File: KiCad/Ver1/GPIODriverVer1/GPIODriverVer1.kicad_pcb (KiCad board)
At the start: 4 copper layers, 176 parts, among them J1 Conn_01x22_Male, J2 GPIODriveOutputs, Q1 DTC143EE, Q10 2N7002, Q11 BSS84, Q12 2N7002, Q13 DTC143EE, Q14 DTC143EE, Q15 DTC143EE, Q16 DTC143EE, Q17 BSS84, Q18 2N7002, Q19 BSS84, Q2 DTC143EE, Q20 2N7002, Q21 BSS84, Q22 2N7002, Q23 BSS84, Q24 2N7002, Q25 2N7002, Q26 2N7002, Q27 2N7002, Q28 2N7002, Q29 2N7002, Q3 DTC143EE, Q30 2N7002, Q31 2N7002, Q32 2N7002, Q4 DTC143EE, Q5 BSS84, Q6 2N7002, Q7 BSS84, Q8 2N7002, Q9 BSS84, U1 74HC244, U2 74HC244, U3 NCV8452, U4 74HC595_Nexperia, U5 74HC595_Nexperia, U6 74HC165

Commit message: Save progress for this week
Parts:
- added REF**: MountingHole_3.2mm_M3_Pad_Via, MountingHole:MountingHole_3.2mm_M3_Pad_Via, F.Cu at (121.2, 125.5)
- added REF**: MountingHole_3.2mm_M3_Pad_Via, MountingHole:MountingHole_3.2mm_M3_Pad_Via, F.Cu at (161.2, 125.5)
- added REF**: MountingHole_3.2mm_M3_Pad_Via, MountingHole:MountingHole_3.2mm_M3_Pad_Via, F.Cu at (121.2, 85.5)
- added REF**: MountingHole_3.2mm_M3_Pad_Via, MountingHole:MountingHole_3.2mm_M3_Pad_Via, F.Cu at (161.2, 85.5)
- Q10, Q12, Q18, Q20, Q22, Q24, Q6, Q8, R29, R30, R31, R32, R34, R36, R38, R40, R53, R54, R55, R56, R58, R60, R62, R64: moved to B.Cu
- moved R64 411.5 mm to (200.8, 167.2), turned to 180 degrees
- moved Q22 408.7 mm to (197.0, 154.8), turned to 180 degrees
- moved Q24 408.4 mm to (196.5, 165.5), turned to 180 degrees
- moved R56 402.5 mm to (201.0, 164.8), turned to 180 degrees
- moved R62 388.5 mm to (201.2, 156.2), turned to 180 degrees
- moved R55 385.2 mm to (201.5, 154.0), turned to 180 degrees
- moved R60 378.7 mm to (201.0, 144.5), turned to 180 degrees
- moved Q20 378.3 mm to (197.0, 143.5), turned to 180 degrees
- moved R58 371.5 mm to (200.0, 129.5), turned to 180 degrees
- moved R53 371.5 mm to (199.8, 126.5), turned to 180 degrees
- moved R54 371.1 mm to (201.5, 141.8), turned to 180 degrees
- moved R45 368.9 mm to (149.2, 120.5), turned to 180 degrees
- moved D23 368.0 mm to (147.0, 119.0)
- moved Q21 367.5 mm to (150.5, 118.5)
- moved Q18 367.1 mm to (196.5, 127.8), turned to 180 degrees
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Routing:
- net VDrive: track 0.00 -> 38.7 mm
- net /DriveSense/D7_In: track 0.00 -> 24.3 mm
- net /DriveSense/D0_In: track 0.00 -> 22.9 mm
- net /DriveSense/D6_In: track 0.00 -> 21.2 mm
- net /DriveSense/D1_In: track 0.00 -> 19.7 mm
- net Net-(D19-Pad2): track 0.00 -> 18.6 mm
- net /DriveSense/D5_In: track 0.00 -> 17.6 mm
- net /DriveSense/D2_In: track 0.00 -> 16.0 mm
- net Net-(D1-Pad2): track 0.00 -> 15.7 mm
- net Net-(D17-Pad2): track 0.00 -> 15.4 mm
- net /DriveSense/D4_In: track 0.00 -> 14.7 mm
- net /DriveSense/D3_In: track 0.00 -> 14.1 mm
- net Net-(D15-Pad2): track 0.00 -> 12.0 mm
- net Net-(D3-Pad2): track 0.00 -> 11.8 mm
- net Net-(D12-Pad2): track 0.00 -> 10.3 mm
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
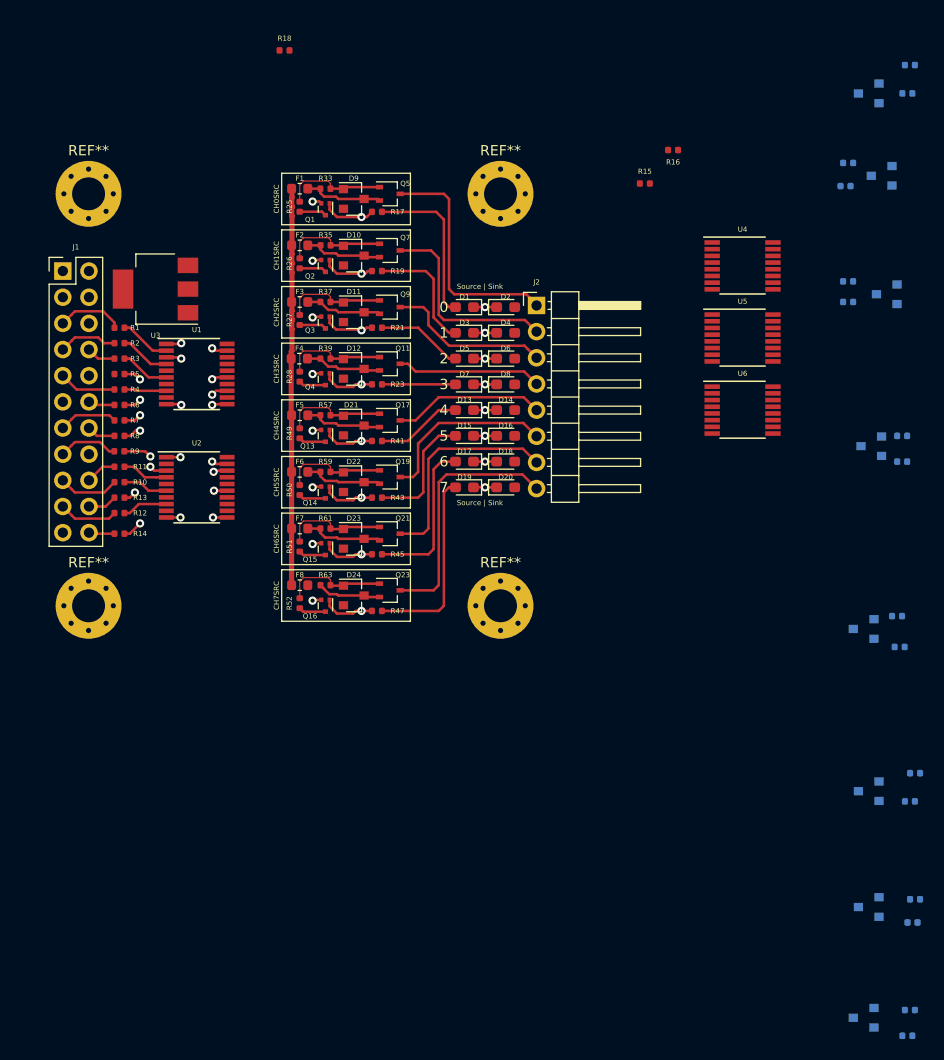
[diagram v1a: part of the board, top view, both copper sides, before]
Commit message: Updated board with possible sink driver layout.
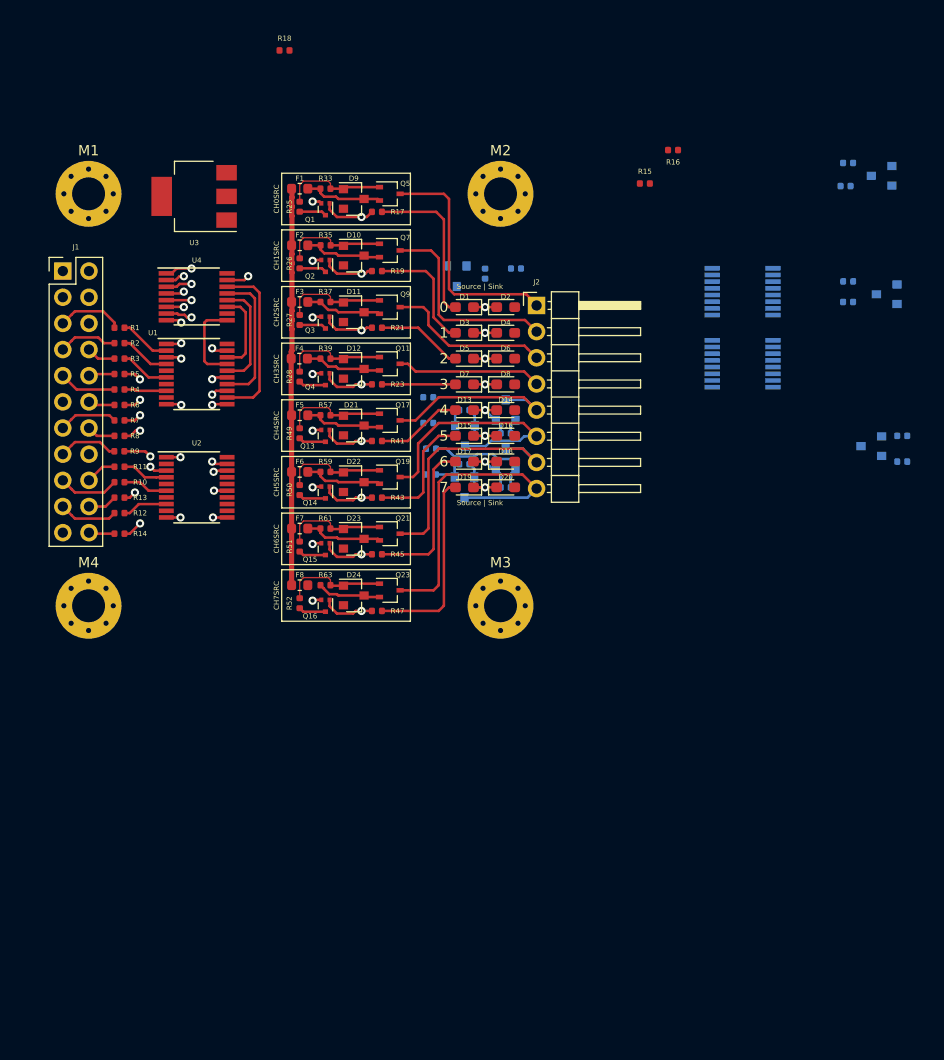
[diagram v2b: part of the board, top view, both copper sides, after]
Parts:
- U5, U6: moved to B.Cu
- moved R64 70.2 mm to (157.7, 111.8)
- moved R56 69.8 mm to (154.5, 112.8)
- moved Q24 64.5 mm to (157.8, 114.0), turned to 270 degrees
- moved R55 64.2 mm to (154.5, 110.2)
- moved R54 58.2 mm to (154.2, 107.8)
- moved R62 57.8 mm to (161.8, 114.0), turned to 0 degrees
- moved R60 57.6 mm to (157.7, 106.5)
- moved Q22 56.0 mm to (161.8, 111.2), turned to 90 degrees
- moved U4 53.1 mm to (131.8, 95.5)
- moved Q20 52.2 mm to (157.8, 109.0), turned to 270 degrees
- moved R53 50.2 mm to (154.2, 105.2)
- moved R34 46.0 mm to (159.8, 93.2), turned to 90 degrees
- moved Q6 43.8 mm to (157.0, 93.5), turned to 270 degrees
- moved R58 43.5 mm to (161.8, 108.8), turned to 0 degrees
- moved R29 41.6 mm to (162.8, 92.8), turned to 0 degrees
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- renumbered REF** to M1, REF** to M2, REF** to M3, REF** to M4
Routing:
- net /OutputDrive/D7_Source: track 5.12 -> 50.7 mm, vias 1 -> 2
- net /OutputDrive/D6_Source: track 5.12 -> 46.3 mm, vias 1 -> 2
- net /OutputDrive/D5_Source: track 5.12 -> 41.5 mm, vias 1 -> 2
- net /OutputDrive/D4_Source: track 5.12 -> 37.0 mm, vias 1 -> 2
- net /OutputDrive/D3_Source: track 5.12 -> 32.5 mm, vias 1 -> 2
- net /OutputDrive/D2_Source: track 5.06 -> 28.2 mm, vias 1 -> 2
- net /OutputDrive/D1_Source: track 5.12 -> 25.5 mm, vias 1 -> 2
- net /OutputDrive/D0_Source: track 5.23 -> 23.3 mm, vias 1 -> 2
- net SrcDriver_DataIn: track 0.00 -> 16.3 mm
- net GND: track 35.3 -> 50.1 mm, vias 23 -> 24
- net SrcDriver_OE: track 0.00 -> 13.6 mm
- net Net-(Q22-Pad1): track 0.00 -> 11.0 mm
- net SrcDriver_LAT: track 0.00 -> 10.6 mm
- net SrcDriver_DataOut: track 0.00 -> 8.36 mm
- net SR_CLK: track 0.00 -> 7.97 mm
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
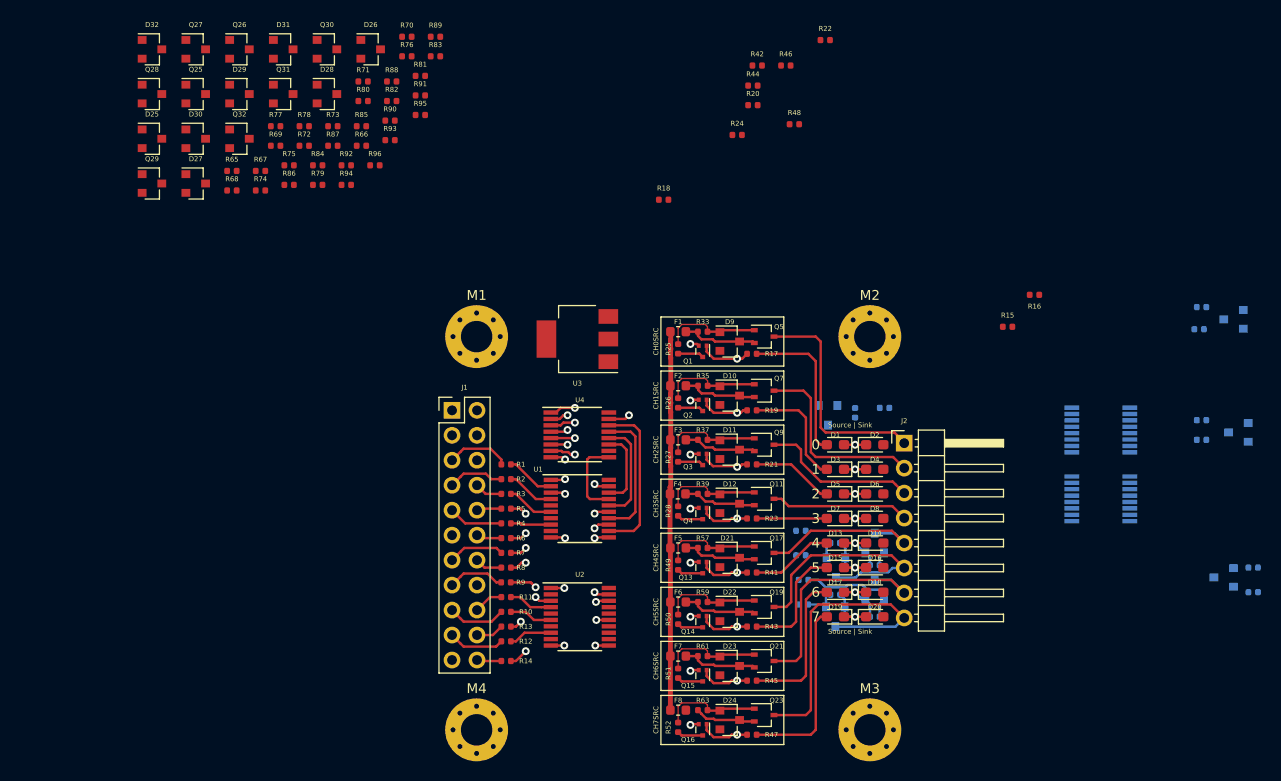
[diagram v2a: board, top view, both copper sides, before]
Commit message: Routed the current sink driver primitives.
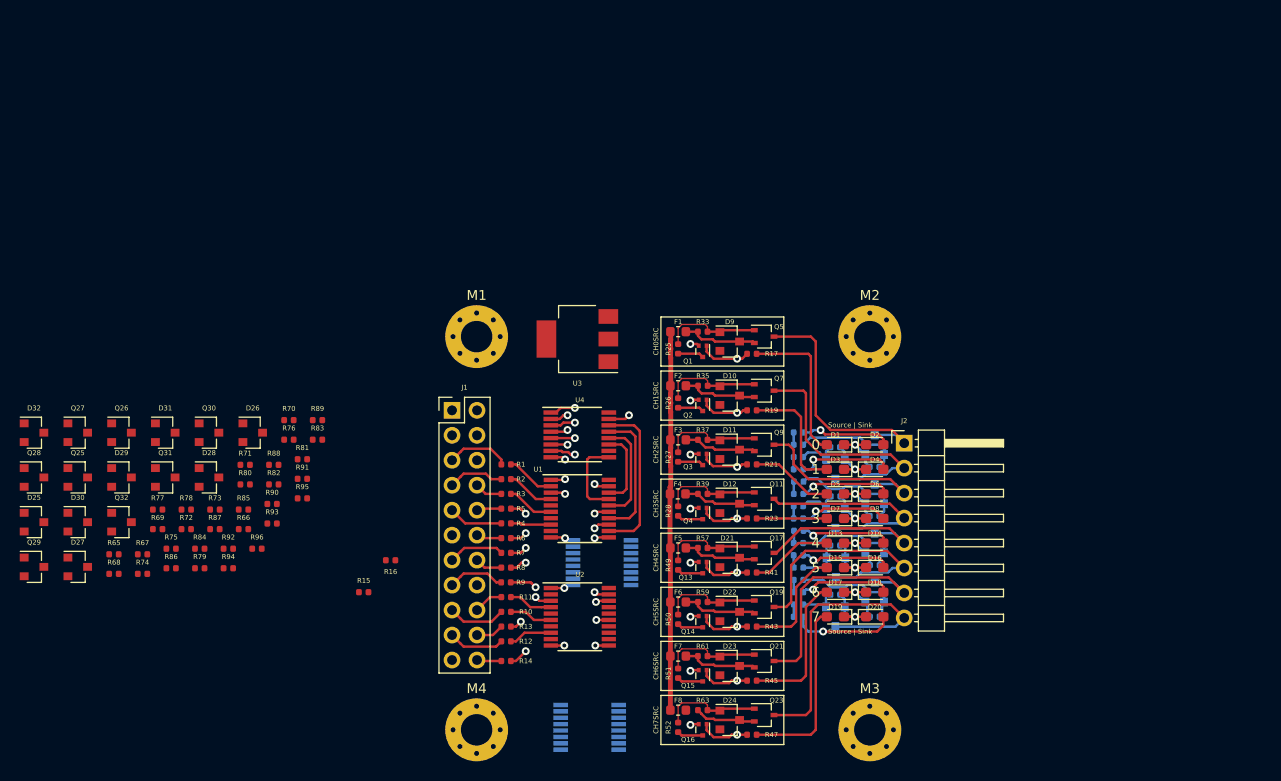
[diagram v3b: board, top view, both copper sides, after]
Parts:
- R18, R20, R22, R24, R42, R44, R46, R48: moved to B.Cu
- moved R16 70.8 mm to (112.5, 108.2)
- moved R15 70.8 mm to (109.8, 111.5)
- moved U5 57.0 mm to (132.8, 125.2)
- moved R46 53.6 mm to (154.0, 111.5), turned to 180 degrees
- moved U6 52.5 mm to (134.0, 108.5)
- moved R48 50.1 mm to (154.0, 114.0), turned to 180 degrees
- moved R44 48.0 mm to (154.0, 107.8), turned to 180 degrees
- moved R42 47.5 mm to (154.0, 105.2), turned to 180 degrees
- moved R32 46.7 mm to (154.0, 102.8)
- moved R22 46.2 mm to (154.0, 101.5), turned to 180 degrees
- moved R30 43.8 mm to (154.0, 97.8)
- moved R40 43.6 mm to (157.8, 101.8)
- moved Q8 43.3 mm to (157.8, 99.0), turned to 270 degrees
- moved R31 41.5 mm to (154.0, 100.2)
- moved R81 40.8 mm to (103.5, 98.0)
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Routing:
- net GND: track 50.1 -> 61.9 mm
- net Net-(Q10-Pad1): track 0.00 -> 11.5 mm
- net Net-(Q6-Pad1): track 0.00 -> 11.1 mm
- net Net-(D20-Pad2): track 0.00 -> 10.5 mm, vias 0 -> 1
- net Net-(D4-Pad2): track 0.00 -> 10.0 mm, vias 0 -> 1
- net Net-(Q18-Pad1): track 1.44 -> 11.0 mm
- net Net-(D18-Pad2): track 0.00 -> 9.44 mm, vias 0 -> 1
- net Net-(D6-Pad2): track 0.00 -> 9.31 mm, vias 0 -> 1
- net Net-(D2-Pad2): track 0.00 -> 9.22 mm, vias 0 -> 1
- net Net-(D16-Pad2): track 0.00 -> 9.22 mm, vias 0 -> 1
- net Net-(D14-Pad2): track 0.00 -> 9.19 mm, vias 0 -> 1
- net Net-(D8-Pad2): track 0.00 -> 9.13 mm, vias 0 -> 1
- net /DriveSense/D3_In: track 14.1 -> 21.5 mm
- net /DriveSense/D1_In: track 19.7 -> 26.8 mm
- net Net-(Q12-Pad1): track 0.00 -> 4.28 mm
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
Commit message: Fanned out/organized the sense circuit
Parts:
- D25, D26, D27, D28, D29, D30, D31, D32, Q25, Q26, Q27, Q28, Q29, Q30, Q31, Q32, R65, R66, R67, R68, R69, R70, R71, R72, R73, R74, R75, R76, R77, R78, R79, R80, R81, R82, R83, R84, R85, R86, R87, R88, R89, R90, R91, R92, R93, R94, R95, R96: moved to B.Cu
- moved R68 59.1 mm to (137.5, 83.8), turned to 180 degrees
- moved D25 57.6 mm to (130.5, 85.0), turned to 180 degrees
- moved R65 57.3 mm to (137.5, 86.2)
- moved Q25 56.8 mm to (135.5, 85.0)
- moved D32 53.0 mm to (107.0, 138.5)
- moved R74 51.1 mm to (133.0, 86.8), turned to 90 degrees
- moved R75 39.3 mm to (102.5, 69.8)
- moved R90 38.8 mm to (97.5, 141.2)
- moved Q32 38.5 mm to (103.0, 138.5)
- moved R71 38.0 mm to (133.0, 84.5), turned to 90 degrees
- moved D31 36.5 mm to (106.3, 127.7)
- moved R66 36.0 mm to (105.7, 70.0)
- moved R69 35.7 mm to (99.5, 71.0)
- moved R92 35.0 mm to (100.5, 141.8)
- moved R72 34.7 mm to (102.2, 72.0)
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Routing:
- net /OutputDrive/D1_Sink: track 1.25 -> 18.2 mm, vias 0 -> 2
- net /OutputDrive/D0_Sink: track 1.25 -> 15.4 mm
- net /OutputDrive/D7_Sink: track 1.26 -> 10.1 mm
- net /OutputDrive/D6_Sink: track 1.25 -> 8.02 mm
- net /OutputDrive/D5_Sink: track 1.26 -> 6.53 mm
- net /OutputDrive/D2_Sink: track 1.26 -> 5.61 mm
- net /OutputDrive/D4_Sink: track 1.26 -> 4.85 mm
- net /OutputDrive/D3_Sink: track 1.25 -> 4.56 mm
- net GND: track 61.9 -> 63.0 mm, vias 24 -> 25
- net /OutputDrive/D7_Source: track 50.7 -> 49.9 mm
- net /OutputDrive/D6_Source: track 46.3 -> 45.6 mm

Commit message: Fully routed Rev 1.0 Prototype Board
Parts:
- R16: moved to B.Cu
- moved R91 59.1 mm to (154.6, 125.3), turned to 180 degrees
- moved R79 58.8 mm to (154.4, 122.2)
- moved R69 58.7 mm to (155.7, 88.0), turned to 180 degrees
- moved R89 56.1 mm to (154.6, 128.1)
- moved R82 55.5 mm to (154.4, 119.2), turned to 180 degrees
- moved R66 54.2 mm to (155.7, 91.0)
- moved R95 53.3 mm to (150.1, 128.1), turned to 90 degrees
- moved R75 53.1 mm to (151.2, 90.8), turned to 90 degrees
- moved R88 53.0 mm to (149.9, 122.0), turned to 90 degrees
- moved R93 51.8 mm to (150.1, 125.9), turned to 90 degrees
- moved R72 51.7 mm to (151.2, 88.5), turned to 90 degrees
- moved R85 50.5 mm to (149.9, 119.7), turned to 90 degrees
- moved Q26 50.3 mm to (153.7, 89.5)
- moved Q31 49.8 mm to (152.6, 126.8)
- moved D26 48.5 mm to (148.7, 89.5), turned to 180 degrees
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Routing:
- net VCC: track 0.00 -> 221.5 mm, vias 0 -> 5
- net GND: track 63.0 -> 142.3 mm, vias 25 -> 31
- net PowerEnable: track 0.00 -> 79.0 mm
- net /DriveSense/D6_Out: track 0.00 -> 55.1 mm
- net /DriveSense/D3_In: track 21.5 -> 71.9 mm, vias 0 -> 2
- net /DriveSense/D4_In: track 18.3 -> 66.2 mm, vias 0 -> 2
- net /DriveSense/D5_Out: track 0.00 -> 47.2 mm
- net /DriveSense/D0_Out: track 0.00 -> 45.0 mm
- net /DriveSense/D2_In: track 19.5 -> 62.4 mm, vias 0 -> 2
- net /DriveSense/D7_Out: track 0.00 -> 42.3 mm, vias 0 -> 2
- net /DriveSense/D1_Out: track 0.00 -> 37.1 mm, vias 0 -> 2
- net SR_CLK: track 7.97 -> 43.6 mm, vias 0 -> 3
- net SinkDriver_DataIn: track 0.00 -> 35.0 mm, vias 0 -> 1
- net SinkDriver_OE: track 0.00 -> 33.7 mm, vias 0 -> 1
- net SinkDriver_LAT: track 0.00 -> 33.3 mm, vias 0 -> 1
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
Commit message: Update gerbers.
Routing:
- net /DriveSense/D7_Out: track 42.3 -> 49.3 mm
- net /DriveSense/D0_Out: track 45.0 -> 39.6 mm
- net /DriveSense/D4_Out: track 23.0 -> 24.8 mm
- net /DriveSense/D4_In: track 66.2 -> 64.6 mm
- net SenseDriver_DataIn: track 26.3 -> 27.5 mm
- net GND: track 142.3 -> 141.3 mm
- net /DriveSense/D1_Out: track 37.1 -> 38.1 mm
- net GPIO_Sink_DI: track 11.2 -> 12.2 mm
- net SrcDriver_DataIn: track 15.5 -> 16.4 mm
- net SinkDriver_DataIn: track 35.0 -> 35.8 mm
- net V+: track 15.9 -> 15.0 mm
- net SinkDriver_LAT: track 33.3 -> 34.1 mm
- net SrcDriver_OE: track 13.0 -> 13.7 mm
- net SinkDriver_OE: track 33.7 -> 34.4 mm
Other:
- board outline added: 50 x 50 mm
- board text added: "8-Channel"
- board text added: "GPIO Driver Version 1.0"
